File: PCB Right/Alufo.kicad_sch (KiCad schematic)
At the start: 32 parts, among them J2 USB_C_Receptacle_USB2.0_16P_2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, J4 USB_C_Receptacle_USB2.0_16P_2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, SW2 BOOT, U2 CH552T, U4 USBLC6-2P6, U6 USBLC6-2P6

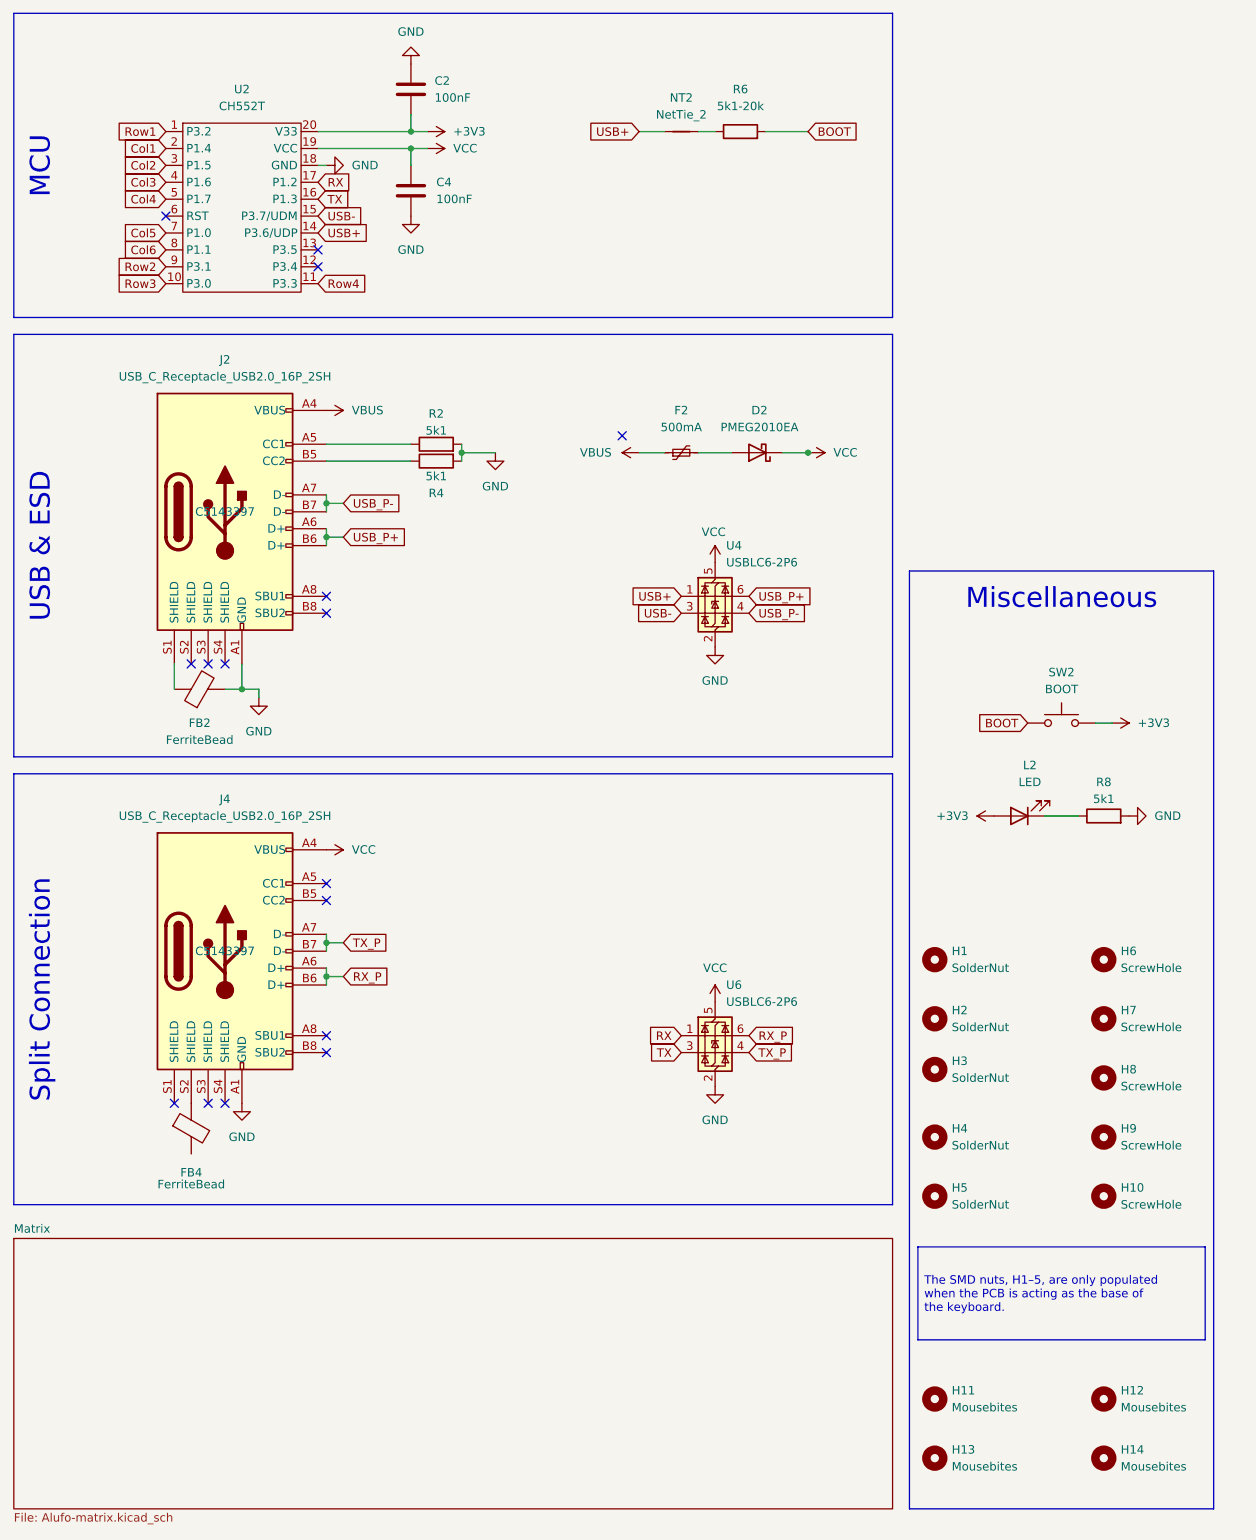
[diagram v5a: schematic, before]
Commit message: Proof-of-concept: One USB C port on right side
The right hand PCB has been setup to have a single USB C port that can handle either bootloader duties or split connection via the side band channels.
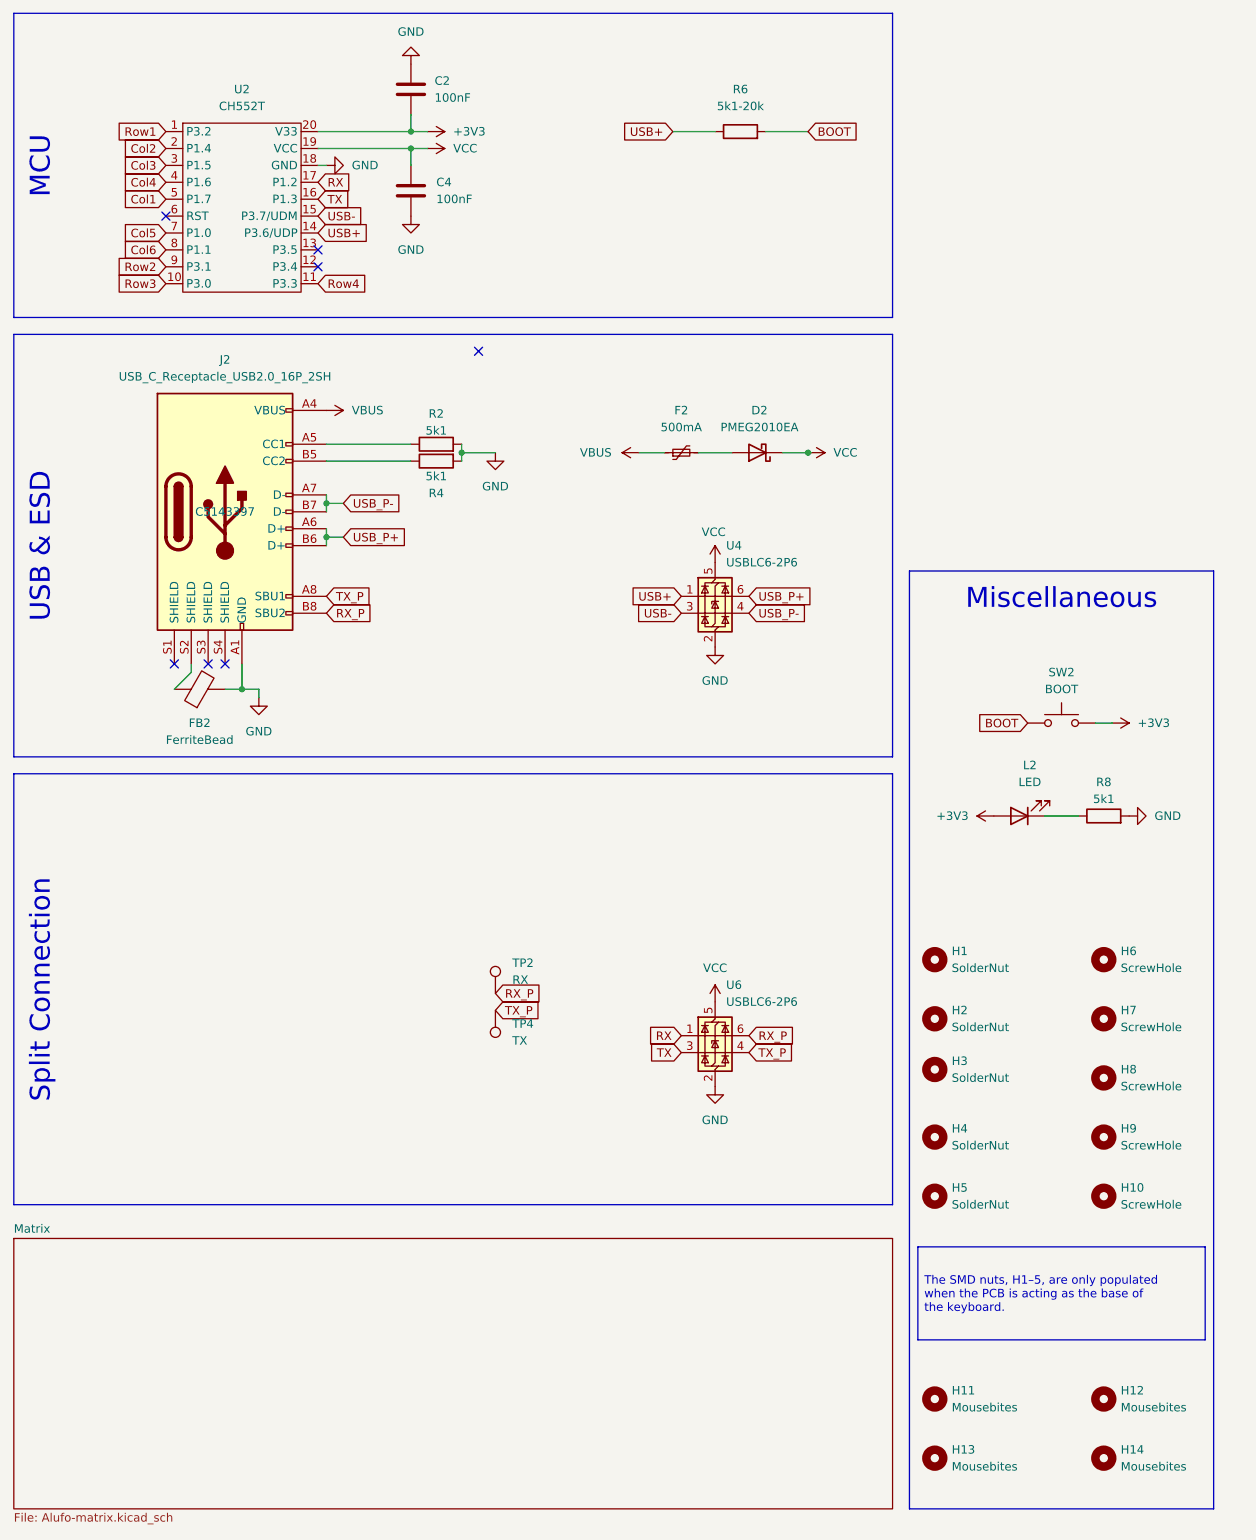
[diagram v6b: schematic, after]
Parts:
- removed FB4: FerriteBead, Inductor_SMD:L_0805_2012Metric, symbol Device:FerriteBead
- removed J4: USB_C_Receptacle_USB2.0_16P_2SH, Project_Library:USB_C_Receptacle_GCT_USB4110, symbol Project_Library:USB_C_Receptacle_USB2.0_16P_2SH
- removed NT2: NetTie_2, Project_Library:NetTie-2_SMD_Pad0.2mm, symbol Device:NetTie_2
- added TP2: RX, TestPoint:TestPoint_Pad_D1.0mm, symbol Connector:TestPoint
- added TP4: TX, TestPoint:TestPoint_Pad_D1.0mm, symbol Connector:TestPoint
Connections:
- net Col1: now also U2.5 (P1.7); no longer U2.2 (P1.4)
- net Col2: now also U2.2 (P1.4); no longer U2.3 (P1.5)
- net Col3: now also U2.3 (P1.5); no longer U2.4 (P1.6)
- net Col4: now also U2.4 (P1.6); no longer U2.5 (P1.7)
- net RX_P: now also J2.B8 (SBU2), TP2.1
- net TX_P: now also J2.A8 (SBU1), TP4.1
- net USB+: now also R6.1
- net at J2.S1 (SHIELD): no longer FB2.1
- net at J2.S2 (SHIELD): now also FB2.1
- no-connect marks 16 -> 7
